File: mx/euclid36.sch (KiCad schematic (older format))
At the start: 87 parts, among them SW10 SW_PUSH, SW11 SW_PUSH, SW12 SW_PUSH, SW14 SW_PUSH, SW15 SW_PUSH, SW16 SW_PUSH, SW17 SW_PUSH, SW18 SW_PUSH, SW19 SW_PUSH, SW2 SW_PUSH, SW20 SW_PUSH, SW21 SW_PUSH, SW22 SW_PUSH, SW23 SW_PUSH, SW25 SW_PUSH, SW26 SW_PUSH, SW27 SW_PUSH, SW28 SW_PUSH, SW29 SW_PUSH, SW3 SW_PUSH, SW31 SW_PUSH, SW32 SW_PUSH, SW33 SW_PUSH, SW34 SW_PUSH, SW35 SW_PUSH, SW37 SW_PUSH, SW38 SW_PUSH, SW39 SW_PUSH, SW4 SW_PUSH, SW40 SW_PUSH, SW41 SW_PUSH, SW42 SW_PUSH, SW5 SW_PUSH, SW6 SW_PUSH, SW8 SW_PUSH, SW9 SW_PUSH, U1 ProMicro

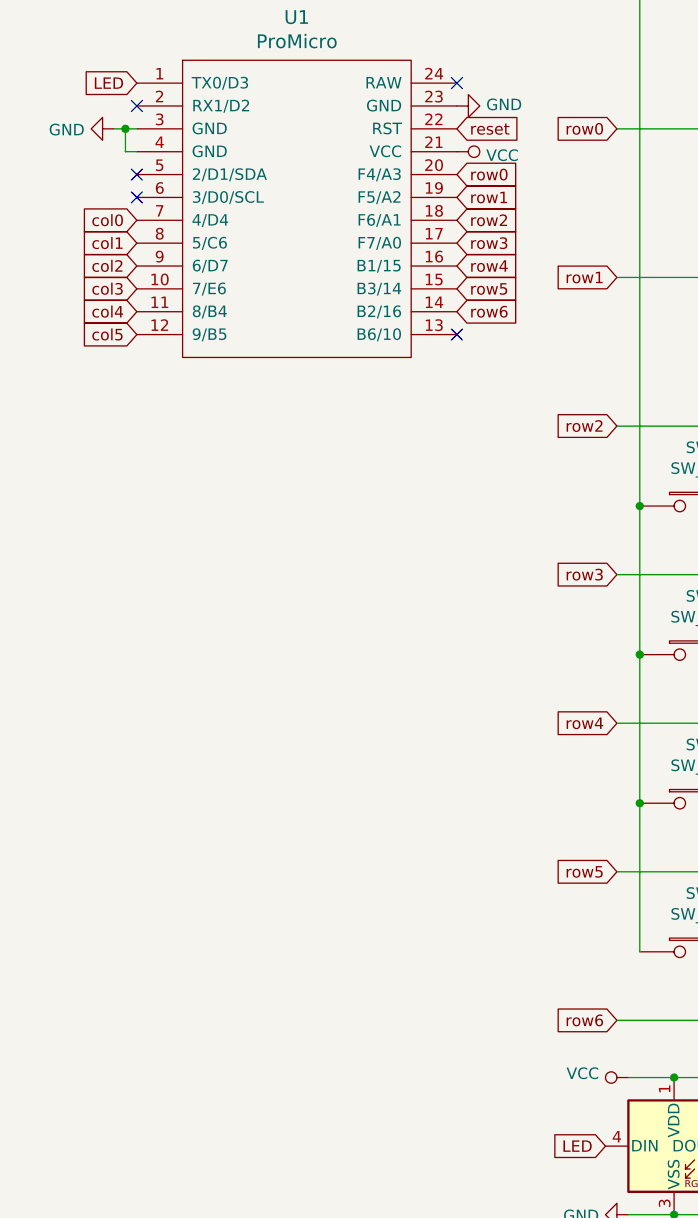
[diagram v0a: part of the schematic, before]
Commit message: added mx sandwich case and updated pcb to support OLED
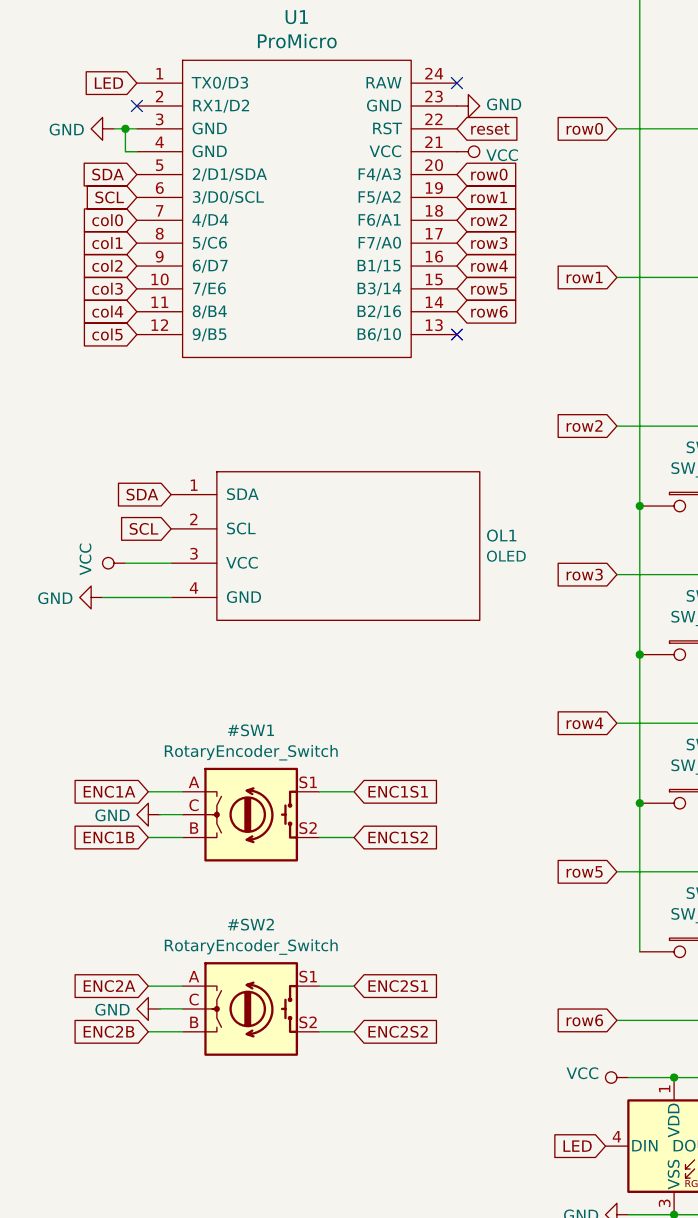
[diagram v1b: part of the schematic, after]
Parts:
- added OL1: OLED, _reviung-kbd:OLED_v2, symbol kbd:OLED
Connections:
- net GND: now also OL1.4 (GND)
- net VCC: now also OL1.3 (VCC)
- net SDA: now reaches U1.5 (2/D1/SDA)
- net SDA: now also OL1.1 (SDA)
- net SCL: now reaches U1.6 (3/D0/SCL)
- net SCL: now also OL1.2 (SCL)
- no-connect marks 6 -> 4
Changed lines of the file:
@@
 $EndComp
 NoConn ~ 1100 1550
-NoConn ~ 1100 1850
-NoConn ~ 1100 1950
 NoConn ~ 2500 1450
 NoConn ~ 2500 2550
@@
 Connection ~ 10050 6400
 NoConn ~ 10950 6100
+$Comp
+L kbd:OLED OL1
+U 1 1 60800FDF
+P 2000 3500
+F 0 "OL1" H 2628 3569 51  0000 L CNN
+F 1 "OLED" H 2628 3479 47  0000 L CNN
+F 2 "_reviung-kbd:OLED_v2" H 2000 3600 60  0001 C CNN
+F 3 "" H 2000 3600 60  0001 C CNN
+	1    2000 3500
+	1    0    0    -1
+$EndComp
+Text GLabel 1100 1850 0    50   Input ~ 0
+SDA
+Text GLabel 1100 1950 0    50   Input ~ 0
+SCL
+Text GLabel 1250 3250 0    50   Input ~ 0
+SDA
+Text GLabel 1250 3400 0    50   Input ~ 0
+SCL
+$Comp
+L power:GND #PWR0101
+U 1 1 60807C4C
+P 950 3700
+F 0 "#PWR0101" H 950 3450 50  0001 C CNN
+F 1 "GND" V 955 3572 50  0000 R CNN
+F 2 "" H 950 3700 50  0001 C CNN
+F 3 "" H 950 3700 50  0001 C CNN
+	1    950  3700
+	0    1    1    0
+$EndComp
+Wire Wire Line
+	1250 3700 950  3700
+Wire Wire Line
+	1250 3550 1050 3550
+$Comp
+L reviung41-rescue:VCC-power #PWR0102
+U 1 1 6081A7F6
+P 1050 3550
+F 0 "#PWR0102" H 1050 3400 50  0001 C CNN
+F 1 "VCC" H 1068 3723 50  0000 C CNN
+F 2 "" H 1050 3550 50  0001 C CNN
+F 3 "" H 1050 3550 50  0001 C CNN
+	1    1050 3550
+	0    -1   -1   0
+$EndComp
+$Comp
+L Device:RotaryEncoder_Switch #SW1
+U 1 1 6081FEB2
+P 1600 4650
+F 0 "#SW1" H 1600 5017 50  0000 C CNN
+F 1 "RotaryEncoder_Switch" H 1600 4926 50  0000 C CNN
+F 2 "" H 1450 4810 50  0001 C CNN
+F 3 "~" H 1600 4910 50  0001 C CNN
+	1    1600 4650
+	1    0    0    -1
+$EndComp
+Text GLabel 2050 4550 2    50   Input ~ 0
+ENC1S1
+Text GLabel 2050 4750 2    50   Input ~ 0
+ENC1S2
+Text GLabel 1150 4550 0    50   Input ~ 0
+ENC1A
+Text GLabel 1150 4750 0    50   Input ~ 0
+ENC1B
+Wire Wire Line
+	1900 4550 2050 4550
+Wire Wire Line
+	1900 4750 2050 4750
+Wire Wire Line
+	1300 4550 1150 4550
+Wire Wire Line
+	1300 4750 1150 4750
+$Comp
+L power:GND #PWR0103
+U 1 1 6083ACEE
+P 1200 4650
+F 0 "#PWR0103" H 1200 4400 50  0001 C CNN
+F 1 "GND" V 1205 4522 50  0000 R CNN
+F 2 "" H 1200 4650 50  0001 C CNN
+F 3 "" H 1200 4650 50  0001 C CNN
+	1    1200 4650
+	0    1    1    0
+$EndComp
+Wire Wire Line
+	1200 4650 1300 4650
+$Comp
+L Device:RotaryEncoder_Switch #SW2
+U 1 1 60847075
+P 1600 5500
+F 0 "#SW2" H 1600 5867 50  0000 C CNN
+F 1 "RotaryEncoder_Switch" H 1600 5776 50  0000 C CNN
+F 2 "" H 1450 5660 50  0001 C CNN
+F 3 "~" H 1600 5760 50  0001 C CNN
+	1    1600 5500
+	1    0    0    -1
+$EndComp
+Text GLabel 2050 5400 2    50   Input ~ 0
+ENC2S1
+Text GLabel 2050 5600 2    50   Input ~ 0
+ENC2S2
+Text GLabel 1150 5400 0    50   Input ~ 0
+ENC2A
+Text GLabel 1150 5600 0    50   Input ~ 0
+ENC2B
+Wire Wire Line
+	1900 5400 2050 5400
+Wire Wire Line
+	1900 5600 2050 5600
+Wire Wire Line
+	1300 5400 1150 5400
+Wire Wire Line
+	1300 5600 1150 5600
+$Comp
+L power:GND #PWR0104
+U 1 1 60847083
+P 1200 5500
+F 0 "#PWR0104" H 1200 5250 50  0001 C CNN
+F 1 "GND" V 1205 5372 50  0000 R CNN
+F 2 "" H 1200 5500 50  0001 C CNN
+F 3 "" H 1200 5500 50  0001 C CNN
+	1    1200 5500
+	0    1    1    0
+$EndComp
+Wire Wire Line
+	1200 5500 1300 5500
 $EndSCHEMATC
